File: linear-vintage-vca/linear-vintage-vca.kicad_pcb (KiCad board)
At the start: 2 copper layers, 50.5 x 110 mm, 57 parts, among them J1 Conn_02x08_Odd_Even, J10 Conn_01x02_Pin, J11 Conn_01x02_Pin, J2 AudioJack2, J3 AudioJack2, J4 AudioJack2, J5 AudioJack2, J6 AudioJack2, J7 AudioJack2, J8 AudioJack2, J9 AudioJack2, Q1 BC556, Q2 BC556, SW1 SW_SPDT_321, SW2 SW_SPDT_321, U1 LM13700, U2 TL072, U3 TL072

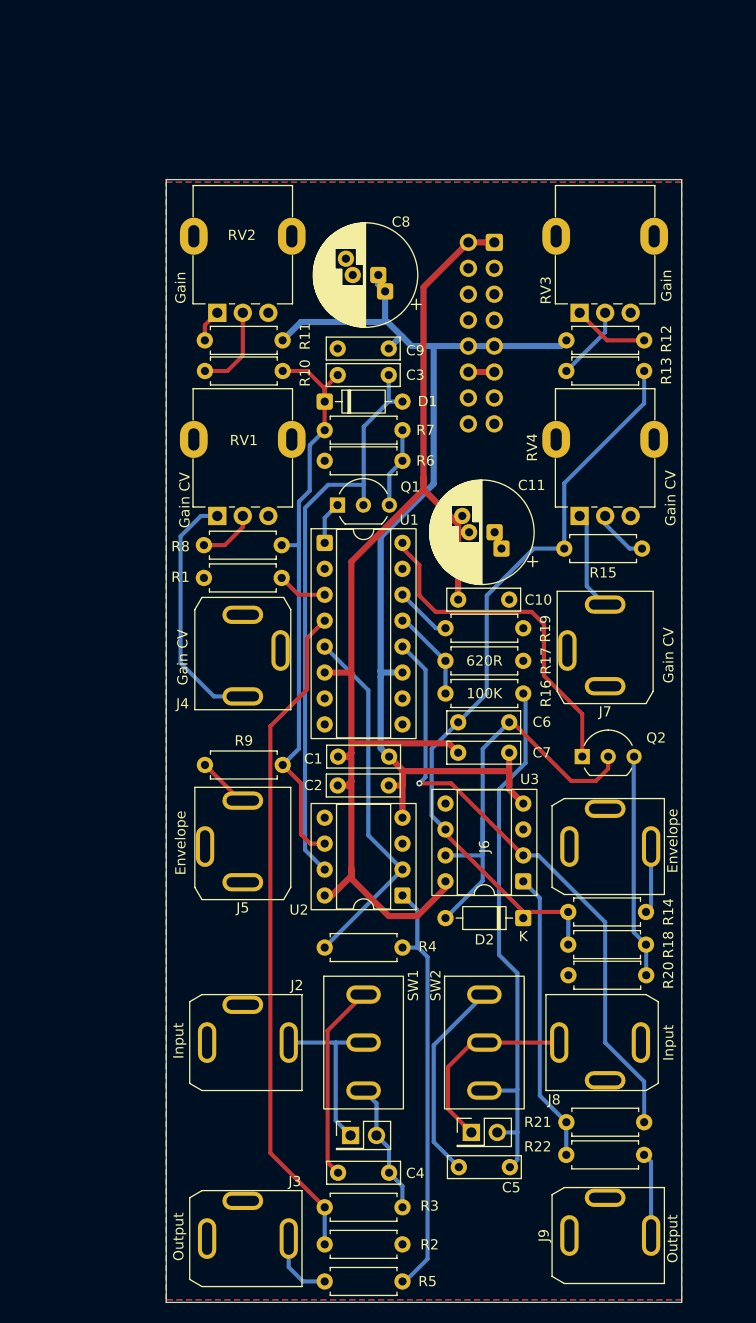
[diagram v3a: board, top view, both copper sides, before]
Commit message: Linear VCA mismatched TL072 power supply fixed.
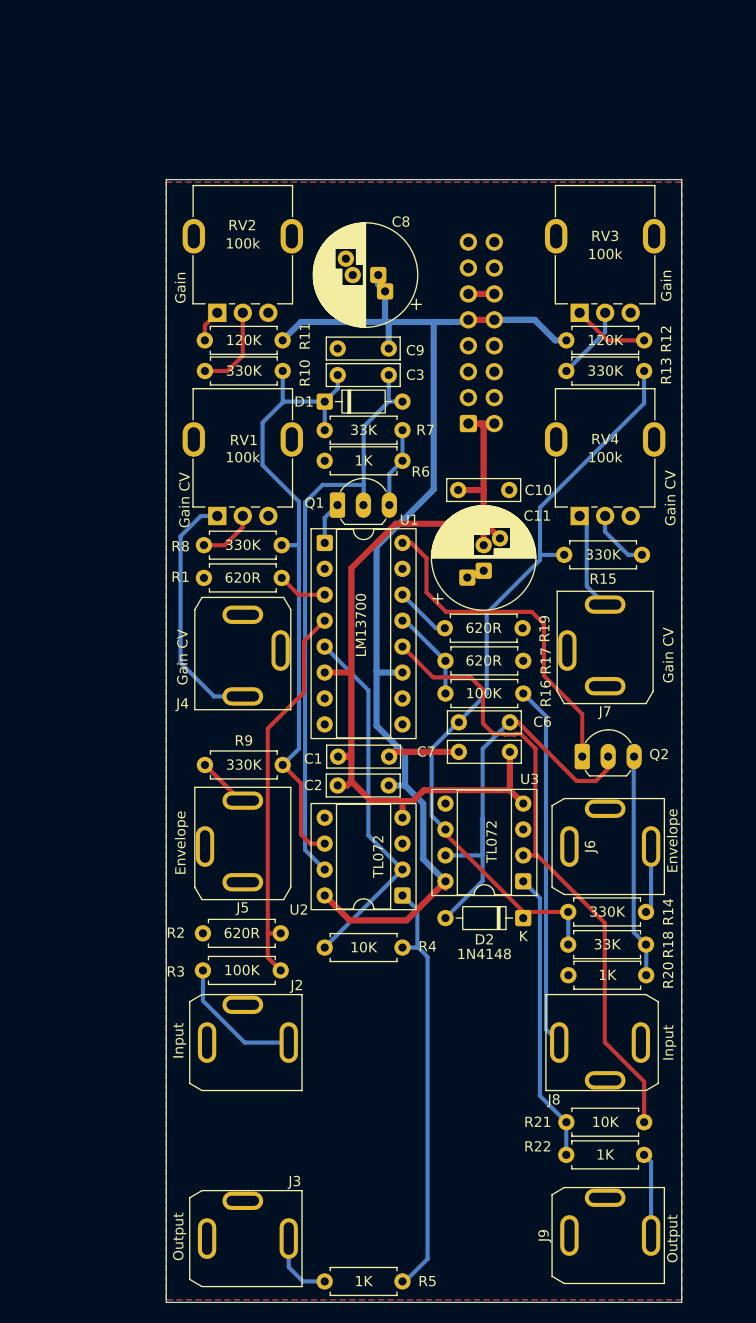
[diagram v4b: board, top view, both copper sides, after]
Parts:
- removed C4, C5: 470n, Capacitor_THT:C_Rect_L7.0mm_W2.0mm_P5.00mm
- removed J10, J11: Conn_01x02_Pin, Connector_PinHeader_2.54mm:PinHeader_2x01_P2.54mm_Vertical
- removed SW1, SW2: SW_SPDT_321, linear_vintage_vca:SPDT_MS-500
- Q1, Q2: footprint Package_TO_SOT_THT:TO-92_Inline_Wide -> linear_vintage_vca:TO-92_Inline_Wide
- moved R2 30.8 mm to (61.2, 133.1), turned to 180 degrees
- moved R3 30.3 mm to (53.6, 136.7), turned to 0 degrees
- moved J1 17.9 mm to (79.6, 83.2), turned to 0 degrees
- moved C10 10.7 mm to (83.6, 89.7)
- moved C7 4.93 mm to (78.7, 115.3), turned to 0 degrees
- moved C11 3.92 mm to (81.1, 97.6), turned to 90 degrees
- moved R15 0.61 mm to (96.6, 96.0)
- moved C6 0.07 mm to (78.7, 112.4)
- moved R19 0.07 mm to (77.3, 103.2)
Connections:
- J2 pad T: Net-(J10-Pin_1) -> Net-(J2-PadT)
- J8 pad T: Net-(J11-Pin_1) -> Net-(J8-PadT)
- R16 pad 1: Net-(J11-Pin_2) -> Net-(J8-PadT)
- R3 pad 1: Net-(J10-Pin_2) -> Net-(J2-PadT)
- U2 pad 4: +12V -> -12V
- U2 pad 8: -12V -> +12V
- U3 pad 4: +12V -> -12V
- U3 pad 8: -12V -> +12V
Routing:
- net Net-(J11-Pin_2): track 53.9 -> 0.00 mm
- net Net-(J8-PadT): track 0.00 -> 35.7 mm
- net -12V: track 117.7 -> 84.6 mm
- net Net-(U1C--): track 65.9 -> 38.7 mm
- net Net-(SW2-C): track 20.0 -> 0.00 mm
- net Net-(SW1-C): track 19.3 -> 0.00 mm
- net Net-(J11-Pin_1): track 19.2 -> 0.00 mm
- net Net-(J10-Pin_1): track 17.0 -> 0.00 mm
- net +12V: track 107.8 -> 124.8 mm
- net Net-(J2-PadT): track 0.00 -> 13.1 mm
- net Net-(J10-Pin_2): track 13.0 -> 0.00 mm
- net Net-(D1-K): track 58.5 -> 63.6 mm
- net Net-(U3A--): track 59.6 -> 61.5 mm, vias 1 -> 0
- net Net-(R15-Pad1): track 5.40 -> 6.89 mm
- net Net-(D2-K): track 75.5 -> 76.2 mm
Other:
- board text added: "ver. 1.2"

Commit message: Fixed OpAmp power rails.
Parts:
- moved R10 7.61 mm to (61.4, 78.1), turned to 180 degrees
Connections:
- RV1 pad 1: Net-(J4-PadT) -> GND
- RV1 pad 3: GND -> Net-(J4-PadT)
- RV2 pad 1: Net-(R11-Pad2) -> GND
- RV2 pad 3: GND -> Net-(R11-Pad2)
- RV3 pad 1: Net-(R12-Pad2) -> GND
- RV3 pad 3: GND -> Net-(R12-Pad2)
- RV4 pad 1: Net-(J7-PadT) -> GND
- RV4 pad 3: GND -> Net-(J7-PadT)
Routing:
- net Net-(D1-K): track 63.6 -> 68.6 mm
- net Net-(R12-Pad2): track 7.44 -> 3.25 mm
- net Net-(R11-Pad2): track 4.21 -> 7.34 mm
- net Net-(J4-PadT): track 24.3 -> 21.7 mm
- net GND: track 0.00 -> 1.99 mm
- net Net-(R10-Pad1): track 8.53 -> 7.29 mm
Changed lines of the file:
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@@
 			(layers "*.Cu" "*.Mask")
 			(remove_unused_layers no)
-			(net 20 "Net-(J4-PadT)")
+			(net 7 "GND")
 			(pinfunction "1")
 			(pintype "passive")
@@
 			(layers "*.Cu" "*.Mask")
 			(remove_unused_layers no)
-			(net 7 "GND")
+			(net 20 "Net-(J4-PadT)")
 			(pinfunction "3")
 			(pintype "passive")
@@
 			(layers "*.Cu" "*.Mask")
 			(remove_unused_layers no)
-			(net 36 "Net-(R12-Pad2)")
+			(net 7 "GND")
 			(pinfunction "1")
 			(pintype "passive")
@@
 			(layers "*.Cu" "*.Mask")
 			(remove_unused_layers no)
-			(net 7 "GND")
+			(net 36 "Net-(R12-Pad2)")
 			(pinfunction "3")
 			(pintype "passive")
@@
 			(layers "*.Cu" "*.Mask")
 			(remove_unused_layers no)
-			(net 23 "Net-(J7-PadT)")
+			(net 7 "GND")
 			(pinfunction "1")
 			(pintype "passive")
@@
 			(layers "*.Cu" "*.Mask")
 			(remove_unused_layers no)
-			(net 7 "GND")
+			(net 23 "Net-(J7-PadT)")
 			(pinfunction "3")
 			(pintype "passive")
@@
 			(layers "*.Cu" "*.Mask")
 			(remove_unused_layers no)
-			(net 35 "Net-(R11-Pad2)")
+			(net 7 "GND")
 			(pinfunction "1")
 			(pintype "passive")
@@
 			(layers "*.Cu" "*.Mask")
 			(remove_unused_layers no)
-			(net 7 "GND")
+			(net 35 "Net-(R11-Pad2)")
 			(pinfunction "3")
 			(pintype "passive")
@@
 		(tags "Resistor Axial_DIN0207 series Axial Horizontal pin pitch 7.62mm 0.25W = 1/4W length 6.3mm diameter 2.5mm")
 		(property "Reference" "R11"
-			(at -2.2 0.4 90)
+			(at -2.608 0.07 90)
 			(layer "F.SilkS")
 			(effects
@@
 	(footprint "linear_vintage_vca:R_Axial_DIN0207_L6.3mm_D2.5mm_P7.62mm_Horizontal"
 		(layer "F.Cu")
-		(at 53.79 78)
+		(at 61.4 78.105 180)
 		(descr "Resistor, Axial_DIN0207 series, Axial, Horizontal, pin pitch=7.62mm, 0.25W = 1/4W, length*diameter=6.3*2.5mm^2, http://cdn-reichelt.de/documents/datenblatt/B400/1_4W%23YAG.pdf")
 		(tags "Resistor Axial_DIN0207 series Axial Horizontal pin pitch 7.62mm 0.25W = 1/4W length 6.3mm diameter 2.5mm")
 		(property "Reference" "R10"
-			(at 9.81 0.2 90)
+			(at -2.608 0 90)
 			(layer "F.SilkS")
 			(effects
@@
 		(attr through_hole)
 		(fp_line
-			(start 0.54 -1.37)
-			(end 7.08 -1.37)
+			(start 7.08 1.37)
+			(end 7.08 1.04)
 			(stroke
 				(width 0.12)
@@
 		)
 		(fp_line
-			(start 0.54 -1.04)
-			(end 0.54 -1.37)
+			(start 7.08 -1.37)
+			(end 7.08 -1.04)
 			(stroke
 				(width 0.12)
@@
 		)
 		(fp_line
-			(start 0.54 1.04)
-			(end 0.54 1.37)
+			(start 0.54 1.37)
+			(end 7.08 1.37)
 			(stroke
 				(width 0.12)
@@
 		)
 		(fp_line
-			(start 0.54 1.37)
-			(end 7.08 1.37)
+			(start 0.54 1.04)
+			(end 0.54 1.37)
 			(stroke
 				(width 0.12)
@@
 		)
 		(fp_line
-			(start 7.08 -1.37)
-			(end 7.08 -1.04)
+			(start 0.54 -1.04)
+			(end 0.54 -1.37)
 			(stroke
 				(width 0.12)
@@
 		)
 		(fp_line
-			(start 7.08 1.37)
-			(end 7.08 1.04)
+			(start 0.54 -1.37)
+			(end 7.08 -1.37)
 			(stroke
 				(width 0.12)
@@
 		)
 		(fp_line
-			(start 0 0)
-			(end 0.66 0)
+			(start 7.62 0)
+			(end 6.96 0)
 			(stroke
 				(width 0.1)
@@
 		)
 		(fp_line
-			(start 7.62 0)
-			(end 6.96 0)
+			(start 0 0)
+			(end 0.66 0)
 			(stroke
 				(width 0.1)
@@
 		)
 		(pad "1" thru_hole circle
-			(at 0 0)
+			(at 0 0 180)
 			(size 1.6 1.6)
 			(drill 0.8)
@@
 		)
 		(pad "2" thru_hole circle
-			(at 7.62 0)
+			(at 7.62 0 180)
 			(size 1.6 1.6)
 			(drill 0.8)
@@
 	)
 	(segment
+		(start 55 73)
+		(end 55 72)
+		(width 0.4)
+		(layer "F.Cu")
+		(net 7)
+	)
+	(segment
+		(start 90.5 92.205)
+		(end 91.2 92.905)
+		(width 0.4)
+		(layer "B.Cu")
+		(net 7)
+	)
+	(segment
 		(start 63.6 124.923634)
 		(end 63.6 90.8701)
@@
 	)
 	(segment
-		(start 61.41 81.084)
-		(end 61.41 78)
+		(start 63 90.8)
+		(end 59.436 87.236)
 		(width 0.4)
 		(layer "B.Cu")
@@
 	)
 	(segment
-		(start 63 90.8)
-		(end 59.436 87.236)
-		(width 0.4)
-		(layer "B.Cu")
-		(net 14)
-	)
-	(segment
 		(start 59.436 87.236)
-		(end 59.436 83.058)
+		(end 59.436 81)
 		(width 0.4)
 		(layer "B.Cu")
@@
 	)
 	(segment
-		(start 61.41 81.084)
-		(end 61.494 81)
+		(start 65.523333 81)
+		(end 59.436 81)
 		(width 0.4)
 		(layer "B.Cu")
@@
 	)
 	(segment
-		(start 61.494 81)
-		(end 65.523333 81)
+		(start 63 115.01)
+		(end 61.41 116.6)
 		(width 0.4)
 		(layer "B.Cu")
@@
 	)
 	(segment
-		(start 63 115.01)
-		(end 61.41 116.6)
+		(start 56.802 81)
+		(end 53.78 77.978)
 		(width 0.4)
 		(layer "B.Cu")
@@
 	)
 	(segment
-		(start 59.436 83.058)
-		(end 61.41 81.084)
+		(start 59.436 81)
+		(end 56.802 81)
 		(width 0.4)
 		(layer "B.Cu")
@@
 	)
 	(segment
-		(start 53.395 92.205)
-		(end 51.4 94.2)
+		(start 59.563 95.631)
+		(end 53.848 101.346)
 		(width 0.4)
-		(layer "B.Cu")
+		(layer "F.Cu")
 		(net 20)
 	)
 	(segment
-		(start 51.4 94.2)
-		(end 51.4 106.6)
+		(start 53.848 101.346)
+		(end 53.848 106.233)
 		(width 0.4)
-		(layer "B.Cu")
+		(layer "F.Cu")
 		(net 20)
 	)
 	(segment
-		(start 55 92.205)
-		(end 53.395 92.205)
+		(start 60 92.205)
+		(end 59.563 92.642)
 		(width 0.4)
-		(layer "B.Cu")
+		(layer "F.Cu")
 		(net 20)
 	)
 	(segment
-		(start 51.4 106.6)
-		(end 54.685 109.885)
+		(start 53.848 106.233)
+		(end 57.5 109.885)
 		(width 0.4)
-		(layer "B.Cu")
+		(layer "F.Cu")
 		(net 20)
 	)
 	(segment
-		(start 54.685 109.885)
-		(end 57.5 109.885)
+		(start 59.563 92.642)
+		(end 59.563 95.631)
 		(width 0.4)
-		(layer "B.Cu")
+		(layer "F.Cu")
 		(net 20)
 	)
@@
 	)
 	(segment
-		(start 90.5 92.205)
-		(end 91.2 92.905)
+		(start 95.25 92.455)
+		(end 95.25 93.472)
 		(width 0.4)
-		(layer "B.Cu")
+		(layer "F.Cu")
 		(net 23)
 	)
 	(segment
-		(start 91.2 99.085)
+		(start 93 95.722)
 		(end 93 100.885)
 		(width 0.4)
-		(layer "B.Cu")
+		(layer "F.Cu")
 		(net 23)
 	)
 	(segment
-		(start 91.2 92.905)
-		(end 91.2 99.085)
+		(start 95.5 92.205)
+		(end 95.25 92.455)
 		(width 0.4)
-		(layer "B.Cu")
+		(layer "F.Cu")
+		(net 23)
+	)
+	(segment
+		(start 95.25 93.472)
+		(end 93 95.722)
+		(width 0.4)
+		(layer "F.Cu")
 		(net 23)
 	)
@@
 	)
 	(segment
-		(start 56 78)
-		(end 53.79 78)
-		(width 0.4)
-		(layer "F.Cu")
-		(net 34)
-	)
-	(segment
-		(start 57.5 76.5)
-		(end 56 78)
+		(start 61.4 77.978)
+		(end 57.5 74.078)
 		(width 0.4)
-		(layer "F.Cu")
+		(layer "B.Cu")
 		(net 34)
 	)
 	(segment
-		(start 57.5 72.3)
-		(end 57.5 76.5)
+		(start 57.5 74.078)
+		(end 57.5 72.3)
 		(width 0.4)
-		(layer "F.Cu")
+		(layer "B.Cu")
 		(net 34)
 	)
 	(segment
-		(start 53.78 73.52)
-		(end 55 72.3)
+		(start 60 72.3)
+		(end 57.3 75)
 		(width 0.4)
 		(layer "F.Cu")
@@
 	)
 	(segment
-		(start 55 73)
-		(end 55 72)
+		(start 57.3 75)
+		(end 53.78 75)
 		(width 0.4)
 		(layer "F.Cu")
@@
 	)
 	(segment
-		(start 53.78 75)
-		(end 53.78 73.52)
+		(start 96.82 73.62)
+		(end 95.5 72.3)
 		(width 0.4)
-		(layer "F.Cu")
-		(net 35)
-	)
-	(segment
-		(start 96.82 75)
-		(end 93.2 75)
-		(width 0.4)
-		(layer "F.Cu")
+		(layer "B.Cu")
 		(net 36)
 	)
 	(segment
-		(start 93.2 75)
-		(end 90.5 72.3)
+		(start 96.82 75)
+		(end 96.82 73.62)
 		(width 0.4)
-		(layer "F.Cu")
+		(layer "B.Cu")
 		(net 36)
 	)

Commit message: VCA v. 2.0
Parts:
- removed C3: 100n, Capacitor_THT:C_Rect_L7.0mm_W2.0mm_P5.00mm
- removed U2: TL072, Package_DIP:DIP-8_W7.62mm_Socket
- added C12: 47uF, Capacitor_THT:CP_Radial_D10.0mm_P2.50mm_P5.00mm, F.Cu at (50.7, 73.7)
- added C5: 100n, Capacitor_THT:C_Rect_L7.0mm_W2.0mm_P5.00mm, F.Cu at (43.9, 113.6)
- added J10: Conn_01x10_Socket, Connector_PinSocket_2.54mm:PinSocket_1x06_P2.54mm_Vertical, F.Cu at (63.9, 116.7)
- added J11: Conn_01x04_Pin, Connector_PinHeader_2.54mm:PinHeader_1x04_P2.54mm_Vertical, B.Cu at (94.5, 45.8)
- added J12: Conn_01x04_Socket, Connector_PinSocket_2.54mm:PinSocket_1x04_P2.54mm_Vertical, F.Cu at (54.5, 45.8)
- added J13: AudioJack2, linear_vintage_vca:Jack_3.5mm_Switch, F.Cu at (84.1, 147.6)
- added J14: AudioJack2, linear_vintage_vca:Jack_3.5mm_Switch, F.Cu at (97.2, 147.6)
- added J15: Conn_02x08_Odd_Even, Connector_IDC:IDC-Header_2x08_P2.54mm_Vertical, B.Cu at (58.9, 76.0)
- added JP1: SolderJumper_2_Open, Jumper:SolderJumper-2_P1.3mm_Open_RoundedPad1.0x1.5mm, F.Cu at (60.2, 49.8)
- added TP1: TestPoint, TestPoint:TestPoint_Loop_D2.54mm_Drill1.5mm_Beaded, F.Cu at (42.1, 79.7)
- added TP2: TestPoint, TestPoint:TestPoint_Loop_D2.54mm_Drill1.5mm_Beaded, F.Cu at (56.8, 85.2)
- added TP3: TestPoint, TestPoint:TestPoint_Loop_D2.54mm_Drill1.5mm_Beaded, F.Cu at (42.0, 85.6)
- added TP4: TestPoint, TestPoint:TestPoint_Loop_D2.54mm_Drill1.5mm_Beaded, F.Cu at (62.3, 85.2)
- C8: value 47uF -> 100n; footprint Capacitor_THT:CP_Radial_D10.0mm_P2.50mm_P5.00mm -> Capacitor_THT:C_Rect_L7.0mm_W2.0mm_P5.00mm
- J1: value Conn_02x08_Odd_Even -> AudioJack2; footprint Connector_IDC:IDC-Header_2x08_P2.54mm_Vertical -> linear_vintage_vca:Jack_3.5mm_Switch; moved to F.Cu
- J2, J3, J4, J5, J6: footprint linear_vintage_vca:Jack_3.5mm_PJ-341-2_Vertical -> linear_vintage_vca:Jack_3.5mm_Switch
- J7, J8: value AudioJack2 -> Conn_01x06_Pin; footprint linear_vintage_vca:Jack_3.5mm_PJ-341-2_Vertical -> Connector_PinHeader_2.54mm:PinHeader_1x06_P2.54mm_Vertical; moved to B.Cu
- J9: value AudioJack2 -> Conn_01x10_Socket; footprint linear_vintage_vca:Jack_3.5mm_PJ-341-2_Vertical -> Connector_PinSocket_2.54mm:PinSocket_1x06_P2.54mm_Vertical
- Q1, Q2: footprint linear_vintage_vca:TO-92_Inline_Wide -> Package_TO_SOT_THT:TO-92_Inline_Wide
- R1, R2: value 620R -> 120K
- R10, R9: value 330K -> 100K
- R11, R12: value 120K -> 620R
- R13, R14: value 330K -> 33K
- R15: value 330K -> 620R
- R16: value 100K -> 620R
- R17: value 620R -> 1K
- R18: value 33K -> 1K
- R19: value 620R -> 10K
- R20: value 1K -> 10K
- R21: value 10K -> 1K
- R3: value 100K -> 330K
- R4: value 10K -> 330K
- R5, R6: value 1K -> 330K
- R7: value 33K -> 330K
- U1: value LM13700 -> TL074; footprint Package_DIP:DIP-16_W7.62mm_Socket -> Package_DIP:DIP-14_W7.62mm_Socket_LongPads
- U3: value TL072 -> LM13700; footprint Package_DIP:DIP-8_W7.62mm_Socket -> Package_DIP:DIP-16_W7.62mm_Socket_LongPads
- moved J3 83.5 mm to (97.2, 89.5), turned to -90 degrees
- moved C8 79.2 mm to (43.8, 143.0), turned to 90 degrees
- moved R2 76.6 mm to (93.3, 63.5), turned to 0 degrees
- moved J9 72.1 mm to (37.5, 116.7), turned to 0 degrees
- moved R12 68.1 mm to (60.6, 136.8), turned to -90 degrees
- moved R21 66.1 mm to (40.8, 116.6), turned to -90 degrees
- moved R11 65.0 mm to (40.8, 136.7), turned to -90 degrees
- moved R5 63.3 mm to (43.8, 111.1), turned to 90 degrees
- moved R15 61.0 mm to (43.8, 126.5), turned to -90 degrees
- moved R18 56.6 mm to (53.0, 90.9)
- moved R13 56.2 mm to (38.0, 101.2), turned to 90 degrees
- moved J4 49.3 mm to (97.2, 134.6), turned to -90 degrees
- moved R10 48.4 mm to (60.6, 126.5), turned to -90 degrees
- moved R22 47.7 mm to (60.6, 116.6), turned to -90 degrees
- moved C11 46.6 mm to (50.7, 62.3), turned to -90 degrees
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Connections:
- C1 pad 1: +12V -> Net-(D1-K)
- C1 pad 2: -12V -> Net-(D1-A)
- C11 pad 1: GND -> +12V
- C11 pad 2: -12V -> GND
- C2 pad 1: +12V -> Net-(D2-K)
- C2 pad 2: -12V -> Net-(D2-A)
- C6 pad 1: Net-(D2-K) -> GND
- C6 pad 2: Net-(D2-A) -> -12V
- C7 pad 2: -12V -> GND
- C8 pad 1: +12V -> GND
- C8 pad 2: GND -> -12V
- J2 pad S: GND -> GND_A
- J2 pad T: Net-(J2-PadT) -> Net-(J7-Pin_5)
- J3 pad S: GND -> GND_A
- J4 pad S: GND -> GND_A
- J4 pad T: Net-(J4-PadT) -> Net-(J8-Pin_5)
- J5 pad S: GND -> GND_A
- J5 pad T: Net-(J5-PadT) -> Net-(J7-Pin_2)
- J6 pad S: GND -> GND_A
- J6 pad T: Net-(J6-PadT) -> Net-(J8-Pin_2)
- R1 pad 1: Net-(U1C-+) -> +12V_A
- R1 pad 2: GND -> Net-(R1-Pad2)
- R10 pad 1: Net-(R10-Pad1) -> Net-(J10-Pin_5)
- R10 pad 2: Net-(D1-K) -> Net-(U3A--)
- R11 pad 1: +12V -> Net-(U3C--)
- R11 pad 2: Net-(R11-Pad2) -> GND
- R12 pad 1: +12V -> Net-(U3A--)
- R12 pad 2: Net-(R12-Pad2) -> GND
- R13 pad 1: Net-(R13-Pad1) -> Net-(D1-K)
- R13 pad 2: Net-(D2-K) -> Net-(Q1-E)
- R14 pad 1: Net-(J6-PadT) -> Net-(D2-K)
- R14 pad 2: Net-(D2-K) -> Net-(Q2-E)
- R15 pad 1: Net-(R15-Pad1) -> Net-(U3C-+)
- R15 pad 2: Net-(D2-K) -> GND
- R16 pad 1: Net-(J8-PadT) -> Net-(U3A-+)
- R16 pad 2: Net-(U1A--) -> GND
- R17 pad 1: Net-(U1A--) -> Net-(Q1-E)
- R18 pad 1: Net-(D2-K) -> Net-(Q2-E)
- R18 pad 2: Net-(Q2-E) -> GND
- R19 pad 1: Net-(U1A-+) -> Net-(U1B--)
- R19 pad 2: GND -> Net-(R19-Pad2)
- R2 pad 1: Net-(U1C--) -> +12V_A
- R2 pad 2: GND -> Net-(R2-Pad2)
- R20 pad 1: Net-(Q2-E) -> Net-(U1C--)
- R20 pad 2: GND -> Net-(R20-Pad2)
- R21 pad 1: Net-(U3A--) -> Net-(R19-Pad2)
- R21 pad 2: Net-(R21-Pad2) -> OUT_1B
- R22 pad 1: Net-(R21-Pad2) -> Net-(R20-Pad2)
- R22 pad 2: Net-(J9-PadT) -> OUT_2B
- R3 pad 1: Net-(J2-PadT) -> Net-(J9-Pin_1)
- R3 pad 2: Net-(U1C--) -> Net-(D1-K)
- R4 pad 1: Net-(U2A--) -> Net-(J9-Pin_2)
- R4 pad 2: Net-(R4-Pad2) -> Net-(D1-K)
- R5 pad 1: Net-(R4-Pad2) -> Net-(J9-Pin_3)
- R5 pad 2: Net-(J3-PadT) -> Net-(D1-K)
- R6 pad 1: Net-(Q1-E) -> Net-(J10-Pin_1)
- R6 pad 2: GND -> Net-(D2-K)
- R7 pad 1: Net-(D1-K) -> Net-(J10-Pin_2)
- R7 pad 2: Net-(Q1-E) -> Net-(D2-K)
- R8 pad 1: Net-(R8-Pad1) -> Net-(J10-Pin_3)
- R8 pad 2: Net-(D1-K) -> Net-(D2-K)
- R9 pad 1: Net-(J5-PadT) -> Net-(J9-Pin_5)
- R9 pad 2: Net-(D1-K) -> Net-(U3C--)
- RV1 pad 1: GND -> GND_A
- RV1 pad 2: Net-(R8-Pad1) -> Net-(J7-Pin_1)
- RV1 pad 3: Net-(J4-PadT) -> Net-(R1-Pad2)
- RV2 pad 1: GND -> GND_A
- RV2 pad 2: Net-(R10-Pad1) -> Net-(J7-Pin_3)
- RV2 pad 3: Net-(R11-Pad2) -> Net-(J1-PadT)
- RV3 pad 1: GND -> GND_A
- RV3 pad 2: Net-(R13-Pad1) -> Net-(J8-Pin_1)
- RV3 pad 3: Net-(R12-Pad2) -> Net-(R2-Pad2)
- RV4 pad 1: GND -> GND_A
- RV4 pad 2: Net-(R15-Pad1) -> Net-(J8-Pin_3)
- RV4 pad 3: Net-(J7-PadT) -> Net-(J3-PadT)
- U1 pad 1: Net-(Q1-C) -> Net-(D1-A)
- U1 pad 11: +12V -> -12V
- U1 pad 12: Net-(U3A--) -> GND
- U1 pad 13: Net-(U1A--) -> Net-(D2-K)
- U1 pad 14: Net-(U1A-+) -> Net-(D2-A)
- U1 pad 2: unconnected-(U1C-DIODE_BIAS-Pad2) -> Net-(D1-K)
- U1 pad 3: Net-(U1C-+) -> GND
- U1 pad 4: Net-(U1C--) -> +12V
- U1 pad 5: Net-(U2A--) -> GND
- U1 pad 6: -12V -> Net-(U1B--)
- U1 pad 7: GND -> Net-(R19-Pad2)
- U1 pad 8: unconnected-(U1-Pad8) -> Net-(R20-Pad2)
- U1 pad 9: unconnected-(U1-Pad9) -> Net-(U1C--)
- U3 pad 1: Net-(R21-Pad2) -> Net-(Q1-C)
- U3 pad 2: Net-(U3A--) -> unconnected-(U3C-DIODE_BIAS-Pad2)
- U3 pad 3: GND -> Net-(U3C-+)
- U3 pad 4: -12V -> Net-(U3C--)
- U3 pad 5: GND -> Net-(U1B--)
- U3 pad 6: Net-(D2-K) -> -12V
- U3 pad 7: Net-(D2-A) -> unconnected-(U3-Pad7)
- U3 pad 8: +12V -> unconnected-(U3-Pad8)
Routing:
- net CV_A: track 0.00 -> 72.4 mm
- net Net-(J7-Pin_1): track 0.00 -> 63.5 mm
- net Net-(J8-Pin_1): track 0.00 -> 62.3 mm
- net Net-(D2-K): track 76.2 -> 20.0 mm
- net Net-(U3A--): track 61.5 -> 10.5 mm
- net Net-(D1-K): track 68.6 -> 20.0 mm
- net Net-(J7-Pin_3): track 0.00 -> 44.1 mm
- net Net-(J8-Pin_3): track 0.00 -> 42.7 mm
- net Net-(R4-Pad2): track 41.8 -> 0.00 mm
- net Net-(U2A--): track 35.8 -> 0.00 mm
- net Net-(J8-PadT): track 35.7 -> 0.00 mm
- net Net-(R21-Pad2): track 28.6 -> 0.00 mm
- net OUT_1A: track 0.00 -> 27.9 mm
- net OUT_2A: track 0.00 -> 27.9 mm
- net +12V_A: track 0.00 -> 24.7 mm
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- added copper zone on B.Cu, net GND_A
- added copper zone on F.Cu, net GND_A
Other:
- board size 50.5 x 110 mm -> 70 x 110 mm
- board text removed: "2025"
- board text removed: "Envelope"
- board text removed: "Gain"
- board text removed: "Gain CV"
- board text removed: "Input"
- board text removed: "Linear VCA"
- board text removed: "Output"
- board text removed: "ver. 1.2"
